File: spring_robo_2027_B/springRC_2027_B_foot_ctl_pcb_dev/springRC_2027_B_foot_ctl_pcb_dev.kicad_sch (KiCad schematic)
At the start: 29 parts, among them J1 Conn_01x22_Pin, J2 USB_C_Receptacle_USB2.0_16P, J3 Conn_01x22_Pin, SW1 SW_Push, SW2 SW_Push, U1 ESP32-S3-WROOM-1, U2 LD1117S33TR_SOT223

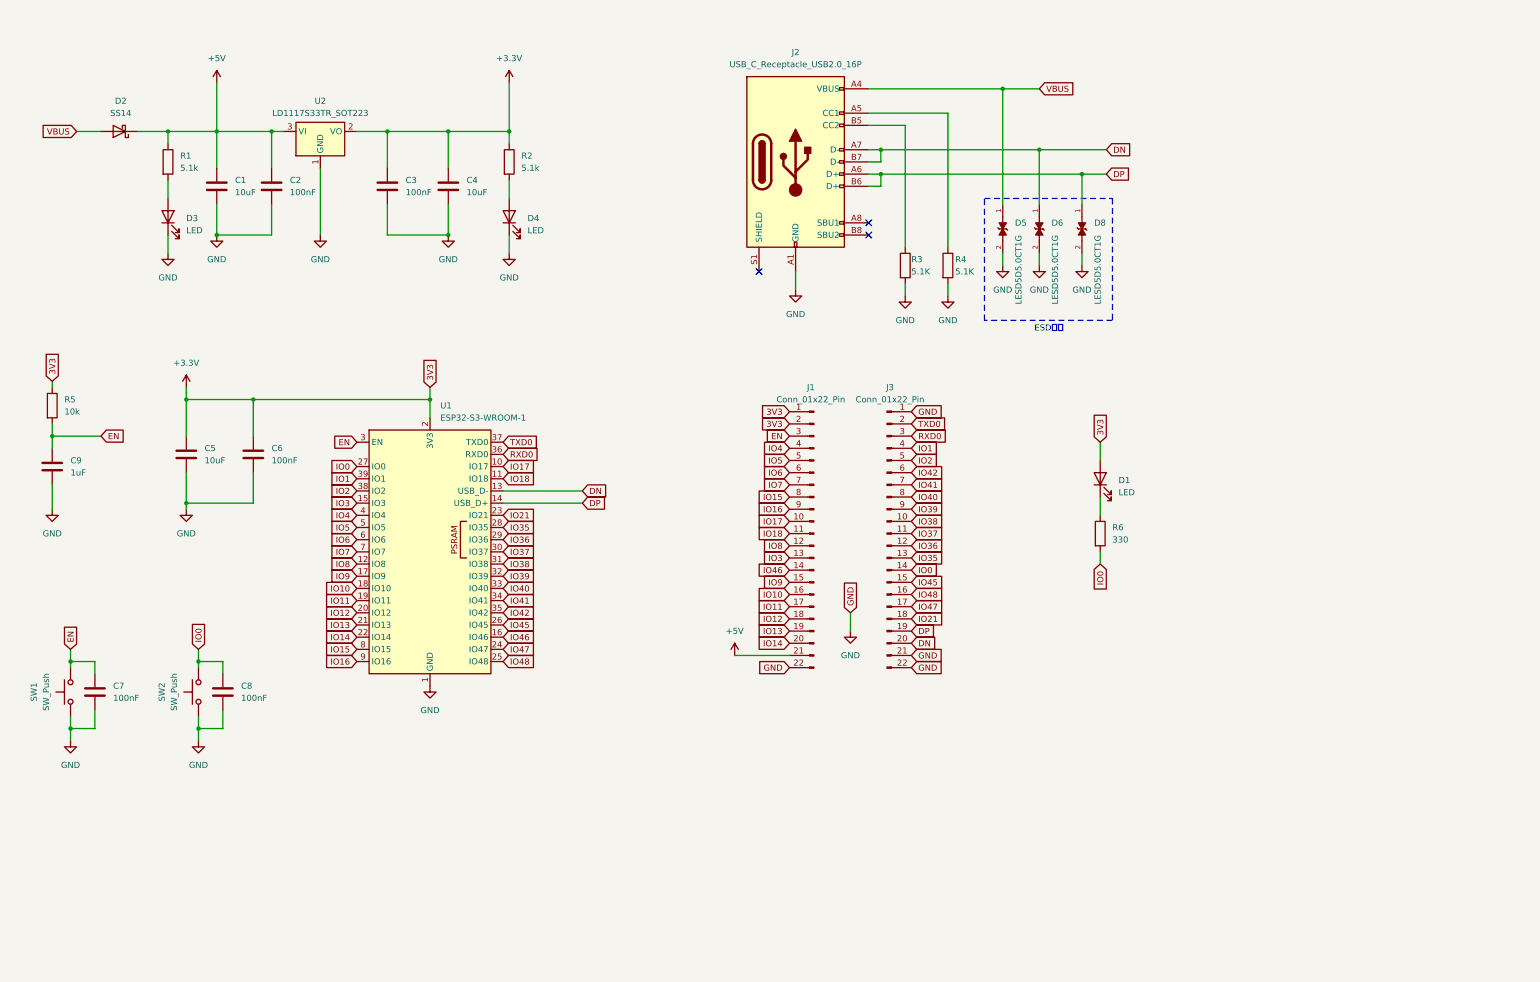
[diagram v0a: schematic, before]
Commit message: 各ピンの割当ひとまず完了　確認後　配線作業
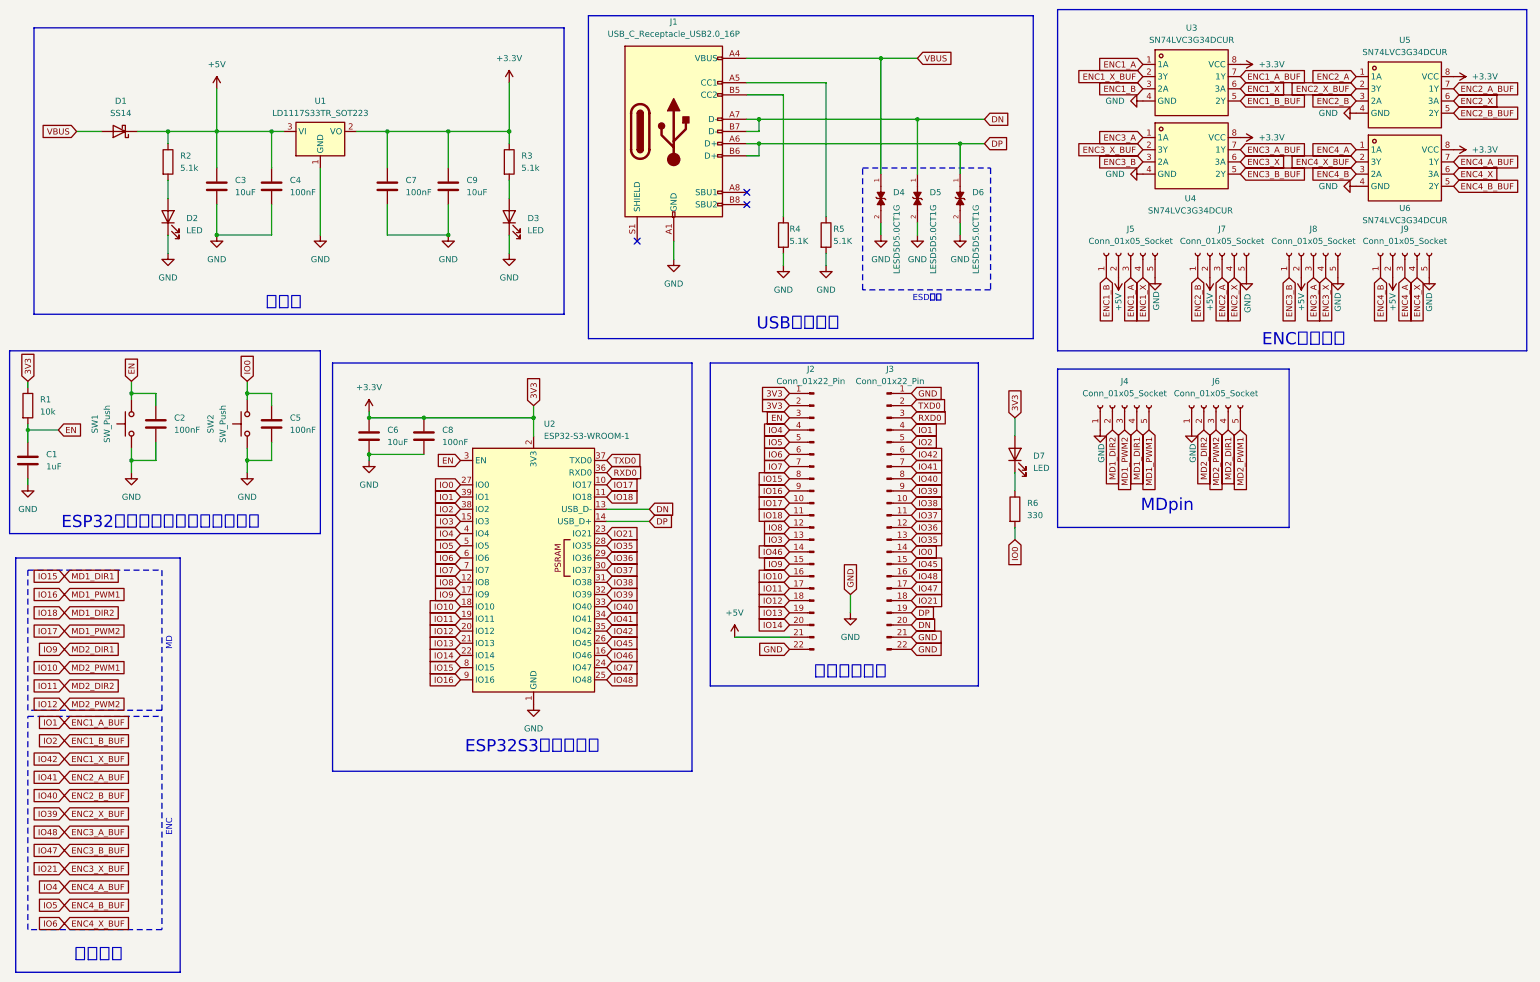
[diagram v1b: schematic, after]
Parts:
- added J4, J5, J6, J7, J8, J9: Conn_01x05_Socket, symbol Connector:Conn_01x05_Socket
- added U3, U4, U5, U6: SN74LVC3G34DCUR, easyeda2kicad:VSSOP-8_L2.1-W2.4-P0.50-LS3.2-BR, symbol imported lib:SN74LVC3G34DCUR
- renumbered C9 to C1, C7 to C2, C1 to C3, C2 to C4, C8 to C5, C5 to C6, C3 to C7, C6 to C8, C4 to C9, D2 to D1, D3 to D2, D4 to D3, D5 to D4, D6 to D5, D8 to D6, D1 to D7, J2 to J1, J1 to J2, R5 to R1, R1 to R2, R2 to R3, R3 to R4, R4 to R5, U2 to U1, U1 to U2
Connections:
- net +3.3V: now also U3.8 (VCC), U4.8 (VCC), U5.8 (VCC), U6.8 (VCC)
- net +5V: now also J5.2 (Pin_2), J7.2 (Pin_2), J8.2 (Pin_2), J9.2 (Pin_2)
- net GND: now also J4.1 (Pin_1), J5.5 (Pin_5), J6.1 (Pin_1), J7.5 (Pin_5), J8.5 (Pin_5), J9.5 (Pin_5), U3.4 (GND), U4.4 (GND), U5.4 (GND), U6.4 (GND)
- net IO10: now also J6.5 (Pin_5)
- net IO11: now also J6.2 (Pin_2)
- net IO12: now also J6.3 (Pin_3)
- net IO15: now also J4.4 (Pin_4)
- net IO16: now also J4.5 (Pin_5)
- net IO17: now also J4.3 (Pin_3)
- net IO18: now also J4.2 (Pin_2)
- net IO9: now also J6.4 (Pin_4)
- net IO1 renamed ENC1_A_BUF
- net ENC1_A_BUF: now also U3.7 (1Y)
- net IO2 renamed ENC1_B_BUF
- net ENC1_B_BUF: now also U3.5 (2Y)
- net IO21 renamed ENC3_X_BUF
- net ENC3_X_BUF: now also U4.2 (3Y)
- net IO39 renamed ENC2_X_BUF
- net ENC2_X_BUF: now also U5.2 (3Y)
- net IO4 renamed ENC4_A_BUF
- net ENC4_A_BUF: now also U6.7 (1Y)
- net IO40 renamed ENC2_B_BUF
- net ENC2_B_BUF: now also U5.5 (2Y)
- net IO41 renamed ENC2_A_BUF
- net ENC2_A_BUF: now also U5.7 (1Y)
- net IO42 renamed ENC1_X_BUF
- net ENC1_X_BUF: now also U3.2 (3Y)
- net IO47 renamed ENC3_B_BUF
- net ENC3_B_BUF: now also U4.5 (2Y)
- net IO48 renamed ENC3_A_BUF
- net ENC3_A_BUF: now also U4.7 (1Y)
- net IO5 renamed ENC4_B_BUF
- net ENC4_B_BUF: now also U6.5 (2Y)
- net IO6 renamed ENC4_X_BUF
- net ENC4_X_BUF: now also U6.2 (3Y)
- new net ENC1_A: J5.3 (Pin_3), U3.1 (1A)
- new net ENC1_B: J5.1 (Pin_1), U3.3 (2A)
- new net ENC1_X: J5.4 (Pin_4), U3.6 (3A)
- new net ENC2_A: J7.3 (Pin_3), U5.1 (1A)
- new net ENC2_B: J7.1 (Pin_1), U5.3 (2A)
- new net ENC2_X: J7.4 (Pin_4), U5.6 (3A)
- new net ENC3_A: J8.3 (Pin_3), U4.1 (1A)
- new net ENC3_B: J8.1 (Pin_1), U4.3 (2A)
- new net ENC3_X: J8.4 (Pin_4), U4.6 (3A)
- new net ENC4_A: J9.3 (Pin_3), U6.1 (1A)
- new net ENC4_B: J9.1 (Pin_1), U6.3 (2A)
- new net ENC4_X: J9.4 (Pin_4), U6.6 (3A)
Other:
- note added: "ENC"
- note added: "ENC信号処理"
- note added: "ESP32S3モジュール"
- note added: "ESP32書き込みリセット周辺回路"
- note added: "MD"
- note added: "MDpin"
- note added: "USB周辺回路"
- note added: "機能割当"
- note added: "汎用コネクタ"
- note added: "電源系"
- moved on the sheet: C1, C2, C5, C6, C8, D4, D5, D6, D7, J1, J2, J3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
